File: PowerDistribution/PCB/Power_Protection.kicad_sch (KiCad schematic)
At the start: 21 parts, among them IC1 SN74LVC1G08DBVR, IC2 SI4162DY-T1-GE3, IC3 TLV1117LV33DCYR, J1 Conn_01x02, J2 Conn_01x02, J3 Conn_01x02, J4 Conn_01x02, Q1 BSS84

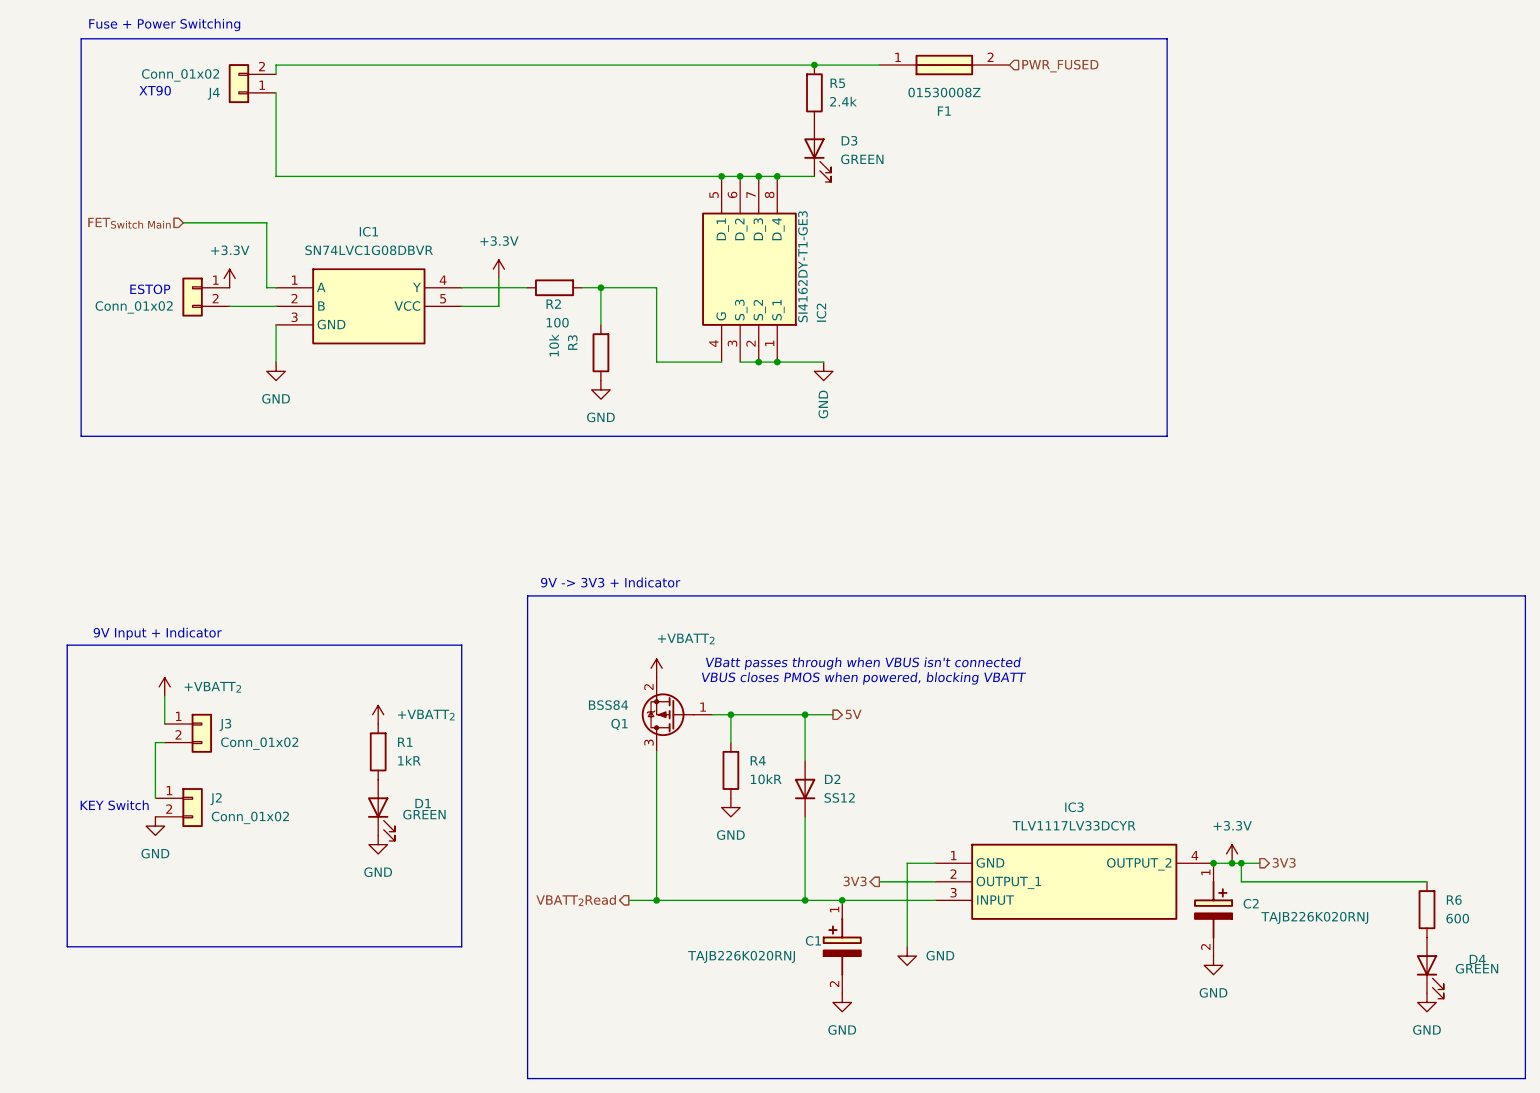
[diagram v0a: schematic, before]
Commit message: Firmware for v2.0, and hardware fixes change for v2.1
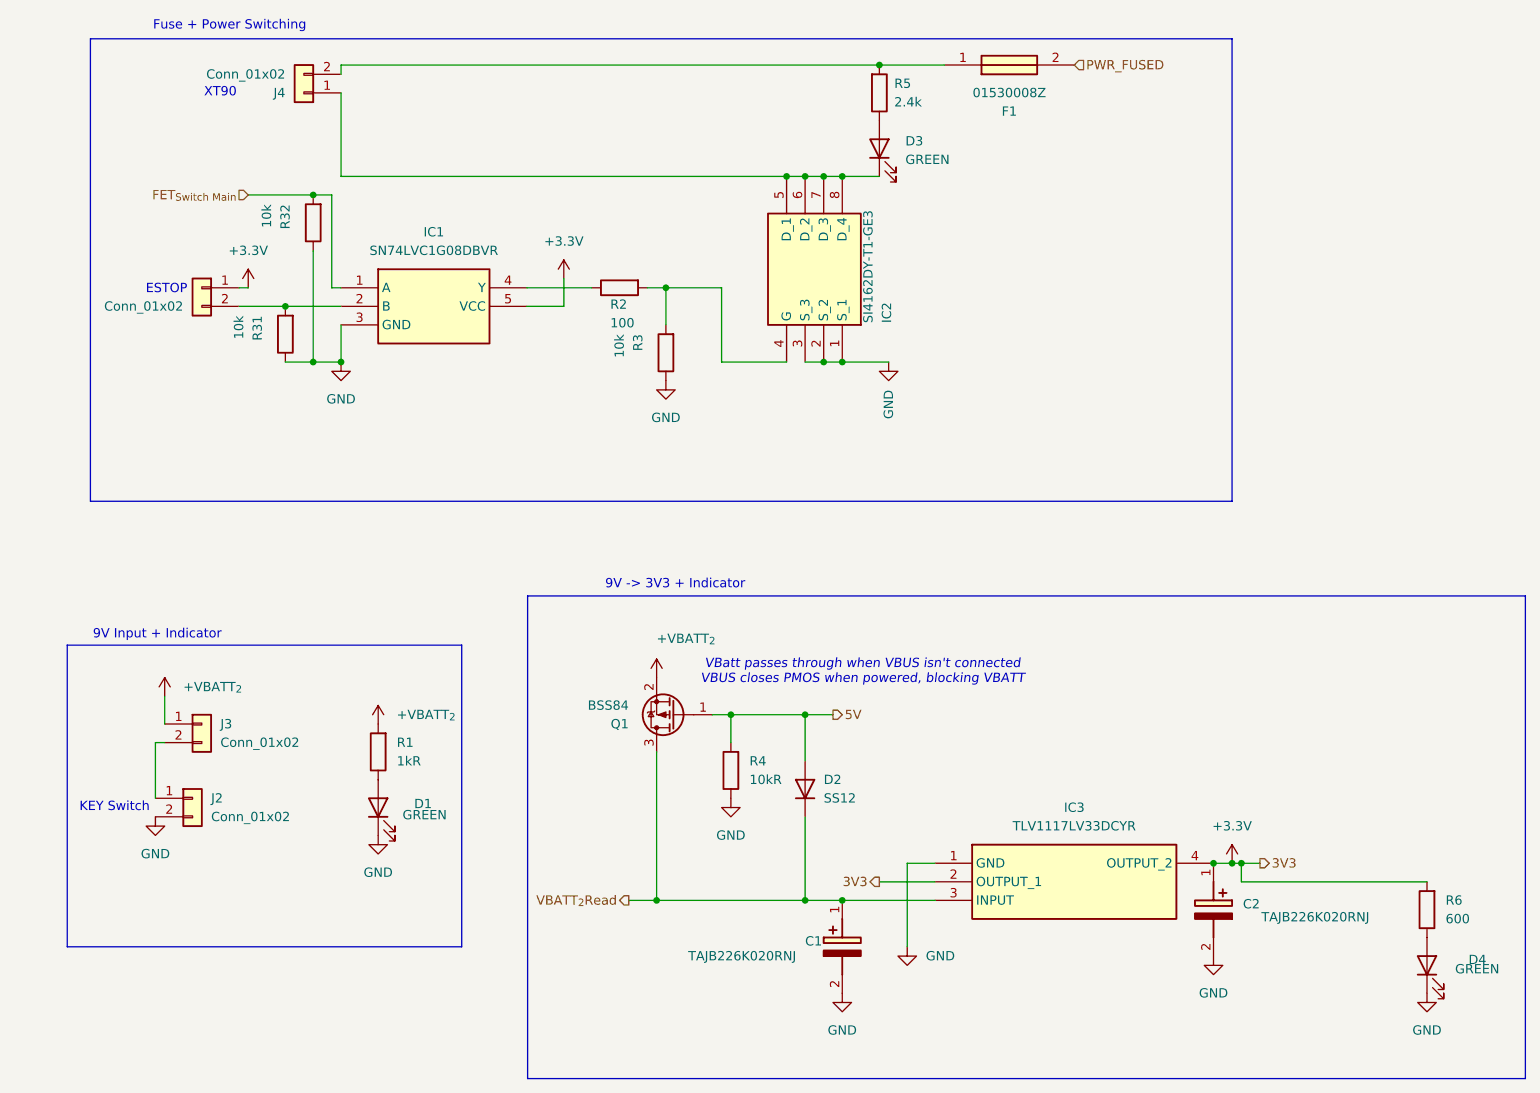
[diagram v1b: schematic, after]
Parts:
- added R31, R32: 10k, Resistor_SMD:R_0402_1005Metric, symbol Device:R
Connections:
- net FET_{Switch Main}: now also R32.2
- net GND: now also R31.1, R32.1
- net at IC1.2 (B), J1.2 (Pin_2): now also R31.2
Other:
- moved on the sheet: D3, F1, IC1, IC2, J4, R2, R3, R5

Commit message: Gitignore fix
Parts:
- C1, C2: footprint CAPPM3528X210N -> Footprints:TAJB226K020RNJ
- F1: footprint 01530008 -> Footprints:01530008
- IC1: footprint SOT95P280X145-5N -> Footprints:SN74LVC1G08DBVR
- IC2: footprint SOIC127P600X175-8N -> Footprints:SI4162DY-T1-GE3
- IC3: footprint SOT230P700X180-4N -> Package_TO_SOT_SMD:SOT-223-3_TabPin2
- J4: footprint Connector_AMASS:AMASS_XT90PW-M_1x02_P10.90mm_Horizontal -> Footprints:AMASS_XT90PW-M
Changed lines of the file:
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@@
 			)
 		)
-		(property "Footprint" "CAPPM3528X210N"
+		(property "Footprint" "Footprints:TAJB226K020RNJ"
 			(at 215.57 144.78 0)
 			(hide yes)
@@
 			)
 		)
-		(property "Footprint" "SOT95P280X145-5N"
+		(property "Footprint" "Footprints:SN74LVC1G08DBVR"
 			(at 72.39 146.99 0)
 			(hide yes)
@@
 			)
 		)
-		(property "Footprint" "Connector_AMASS:AMASS_XT90PW-M_1x02_P10.90mm_Horizontal"
+		(property "Footprint" "Footprints:AMASS_XT90PW-M"
 			(at 45.72 25.4 0)
 			(hide yes)
@@
 			)
 		)
-		(property "Footprint" "01530008"
+		(property "Footprint" "Footprints:01530008"
 			(at 147.32 -74.6 0)
 			(hide yes)
@@
 			)
 		)
-		(property "Footprint" "CAPPM3528X210N"
+		(property "Footprint" "Footprints:TAJB226K020RNJ"
 			(at 73.99 139.7 0)
 			(hide yes)
@@
 			)
 		)
-		(property "Footprint" "SOT230P700X180-4N"
+		(property "Footprint" "Package_TO_SOT_SMD:SOT-223-3_TabPin2"
 			(at 166.37 225.73 0)
 			(hide yes)
@@
 			)
 		)
-		(property "Footprint" "SOIC127P600X175-8N"
+		(property "Footprint" "Footprints:SI4162DY-T1-GE3"
 			(at 24.46 40.64 0)
 			(hide yes)
